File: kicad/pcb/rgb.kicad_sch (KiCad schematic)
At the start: 13 parts

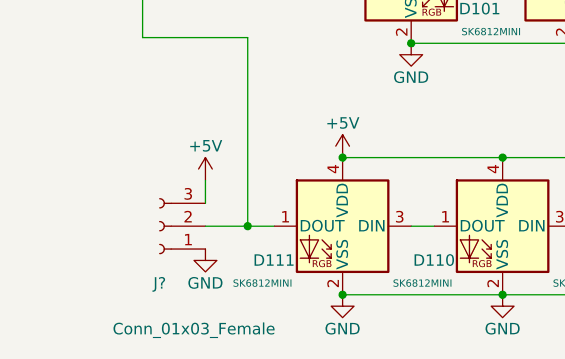
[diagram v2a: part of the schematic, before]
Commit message: Remove extra mounting holes from PCB and update version number.
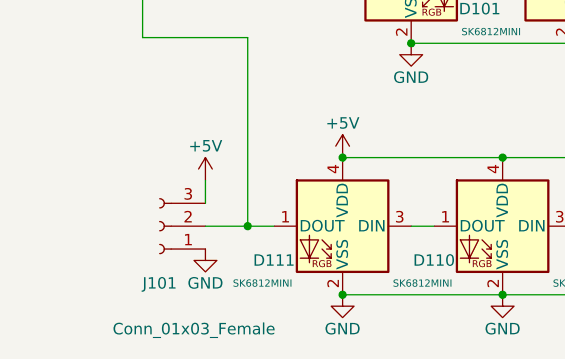
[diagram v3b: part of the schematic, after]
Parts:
- gave numbers to parts that had none: 1
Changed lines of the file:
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@@
   (title_block
     (title "Le Capybara")
-    (date "2023-09-01")
-    (rev "0.2")
+    (date "2024-02-21")
+    (rev "1.0")
     (company "sporkus")
   )
@@
   (symbol (lib_id "LeChiffre-rescue:Conn_01x03_Female-Connector") (at 73.025 89.535 0) (mirror y) (unit 1)
     (in_bom yes) (on_board yes) (dnp no)
-    (property "Reference" "J?" (at 73.025 95.885 0)
+    (property "Reference" "J101" (at 73.025 95.885 0)
       (effects (font (size 1.27 1.27)))
     )
@@
     (instances
       (project "le_capybara"
-        (path "/ca0d59d2-7f9b-4344-99bc-39bc2c8c88cb/9412d715-f7b7-4535-9cc7-549a2178ec10"
-          (reference "J?") (unit 1)
-        )
         (path "/ca0d59d2-7f9b-4344-99bc-39bc2c8c88cb/ddb59433-fe5b-4efc-b099-e8e1feecfd95"
           (reference "J101") (unit 1)
@@
   (symbol (lib_id "power:GND") (at 78.105 92.075 0) (mirror y) (unit 1)
     (in_bom yes) (on_board yes) (dnp no)
-    (property "Reference" "#PWR?" (at 78.105 98.425 0)
+    (property "Reference" "#PWR0105" (at 78.105 98.425 0)
       (effects (font (size 1.27 1.27)) hide)
     )
@@
     (instances
       (project "le_capybara"
-        (path "/ca0d59d2-7f9b-4344-99bc-39bc2c8c88cb/9412d715-f7b7-4535-9cc7-549a2178ec10"
-          (reference "#PWR?") (unit 1)
-        )
         (path "/ca0d59d2-7f9b-4344-99bc-39bc2c8c88cb/ddb59433-fe5b-4efc-b099-e8e1feecfd95"
           (reference "#PWR0105") (unit 1)
@@
   (symbol (lib_id "power:GND") (at 100.965 69.215 0) (mirror y) (unit 1)
     (in_bom yes) (on_board yes) (dnp no)
-    (property "Reference" "#PWR?" (at 100.965 75.565 0)
+    (property "Reference" "#PWR0102" (at 100.965 75.565 0)
       (effects (font (size 1.27 1.27)) hide)
     )
@@
     (instances
       (project "le_capybara"
-        (path "/ca0d59d2-7f9b-4344-99bc-39bc2c8c88cb/9412d715-f7b7-4535-9cc7-549a2178ec10"
-          (reference "#PWR?") (unit 1)
-        )
         (path "/ca0d59d2-7f9b-4344-99bc-39bc2c8c88cb/ddb59433-fe5b-4efc-b099-e8e1feecfd95"
           (reference "#PWR0102") (unit 1)
@@
   (symbol (lib_id "power:GND") (at 93.345 97.155 0) (mirror y) (unit 1)
     (in_bom yes) (on_board yes) (dnp no)
-    (property "Reference" "#PWR?" (at 93.345 103.505 0)
+    (property "Reference" "#PWR0106" (at 93.345 103.505 0)
       (effects (font (size 1.27 1.27)) hide)
     )
@@
     (instances
       (project "le_capybara"
-        (path "/ca0d59d2-7f9b-4344-99bc-39bc2c8c88cb/9412d715-f7b7-4535-9cc7-549a2178ec10"
-          (reference "#PWR?") (unit 1)
-        )
         (path "/ca0d59d2-7f9b-4344-99bc-39bc2c8c88cb/ddb59433-fe5b-4efc-b099-e8e1feecfd95"
           (reference "#PWR0106") (unit 1)
@@
   (symbol (lib_id "power:GND") (at 111.125 97.155 0) (mirror y) (unit 1)
     (in_bom yes) (on_board yes) (dnp no)
-    (property "Reference" "#PWR?" (at 111.125 103.505 0)
+    (property "Reference" "#PWR0107" (at 111.125 103.505 0)
       (effects (font (size 1.27 1.27)) hide)
     )
@@
     (instances
       (project "le_capybara"
-        (path "/ca0d59d2-7f9b-4344-99bc-39bc2c8c88cb/9412d715-f7b7-4535-9cc7-549a2178ec10"
-          (reference "#PWR?") (unit 1)
-        )
         (path "/ca0d59d2-7f9b-4344-99bc-39bc2c8c88cb/ddb59433-fe5b-4efc-b099-e8e1feecfd95"
           (reference "#PWR0107") (unit 1)
